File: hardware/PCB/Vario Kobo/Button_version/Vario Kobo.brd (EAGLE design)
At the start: 78.1 x 17.1 mm, 24 parts

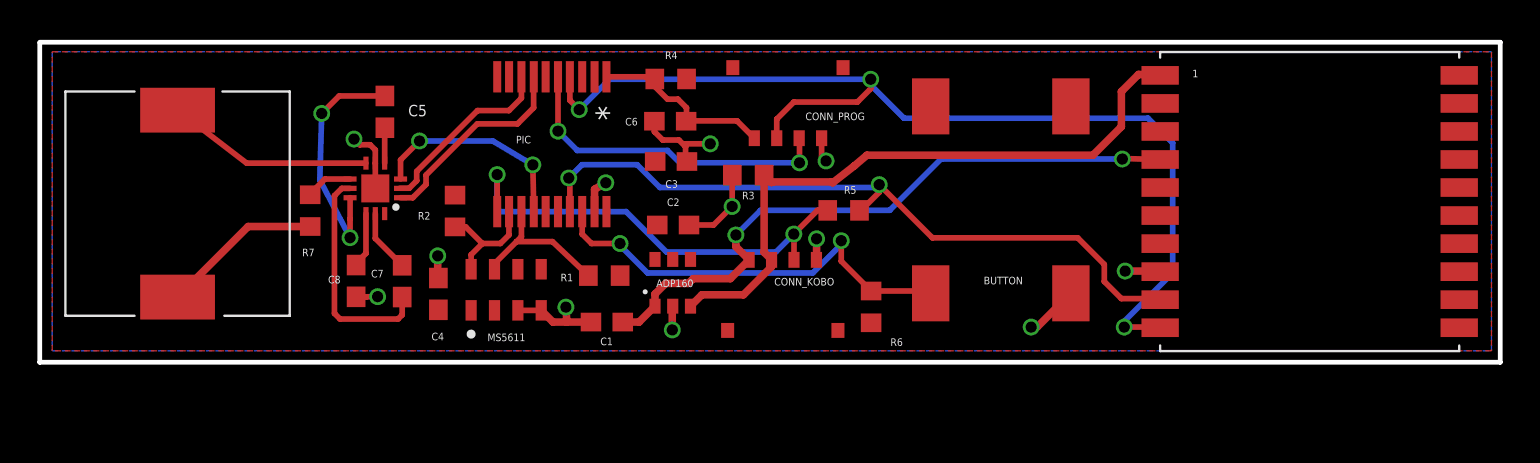
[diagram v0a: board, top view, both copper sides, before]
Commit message: CLEAN
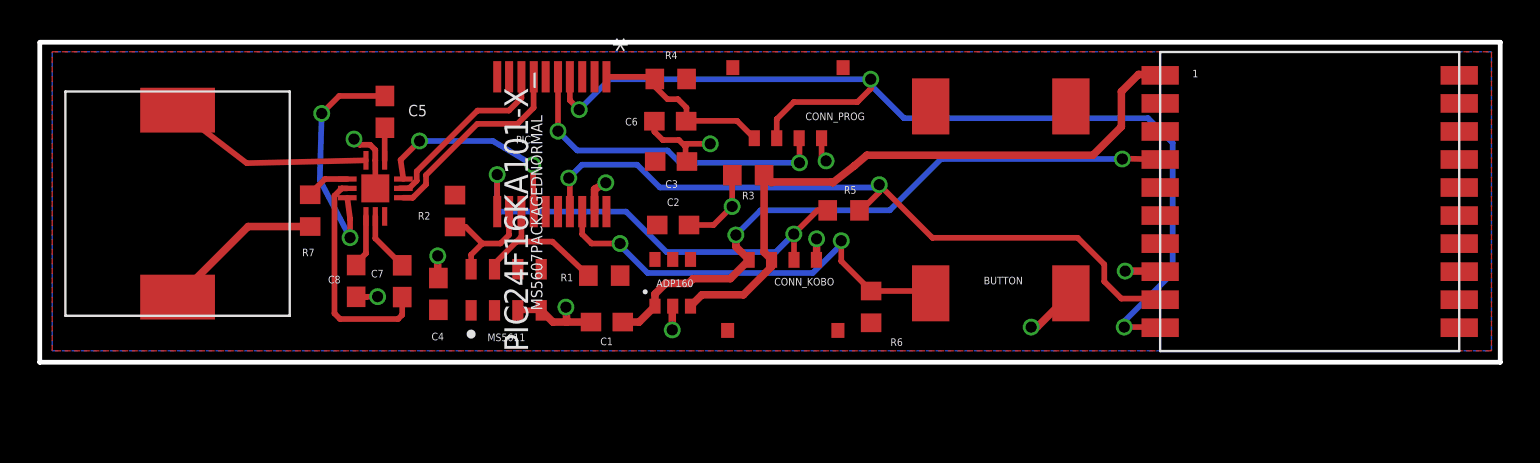
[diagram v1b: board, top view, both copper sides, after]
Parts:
- MAS: device mas:QFN12_3X3 -> mas:QFN12_3X3_LONGPADS
- MS5611: value (none) -> MS5607PACKAGEDNORMAL
- PIC: value (none) -> PIC24F16KA101-X_
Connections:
- net GND: now also MS5611.3, MS5611.4; no longer MS5611.P$3, MS5611.P$4
- net PROUT: now also MS5611.1, MS5611.2; no longer MS5611.P$1, MS5611.P$2
- net SCL: now also MS5611.8; no longer MS5611.P$8
- net SDA: now also MS5611.7; no longer MS5611.P$7
